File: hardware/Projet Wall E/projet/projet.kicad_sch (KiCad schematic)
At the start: 0 parts

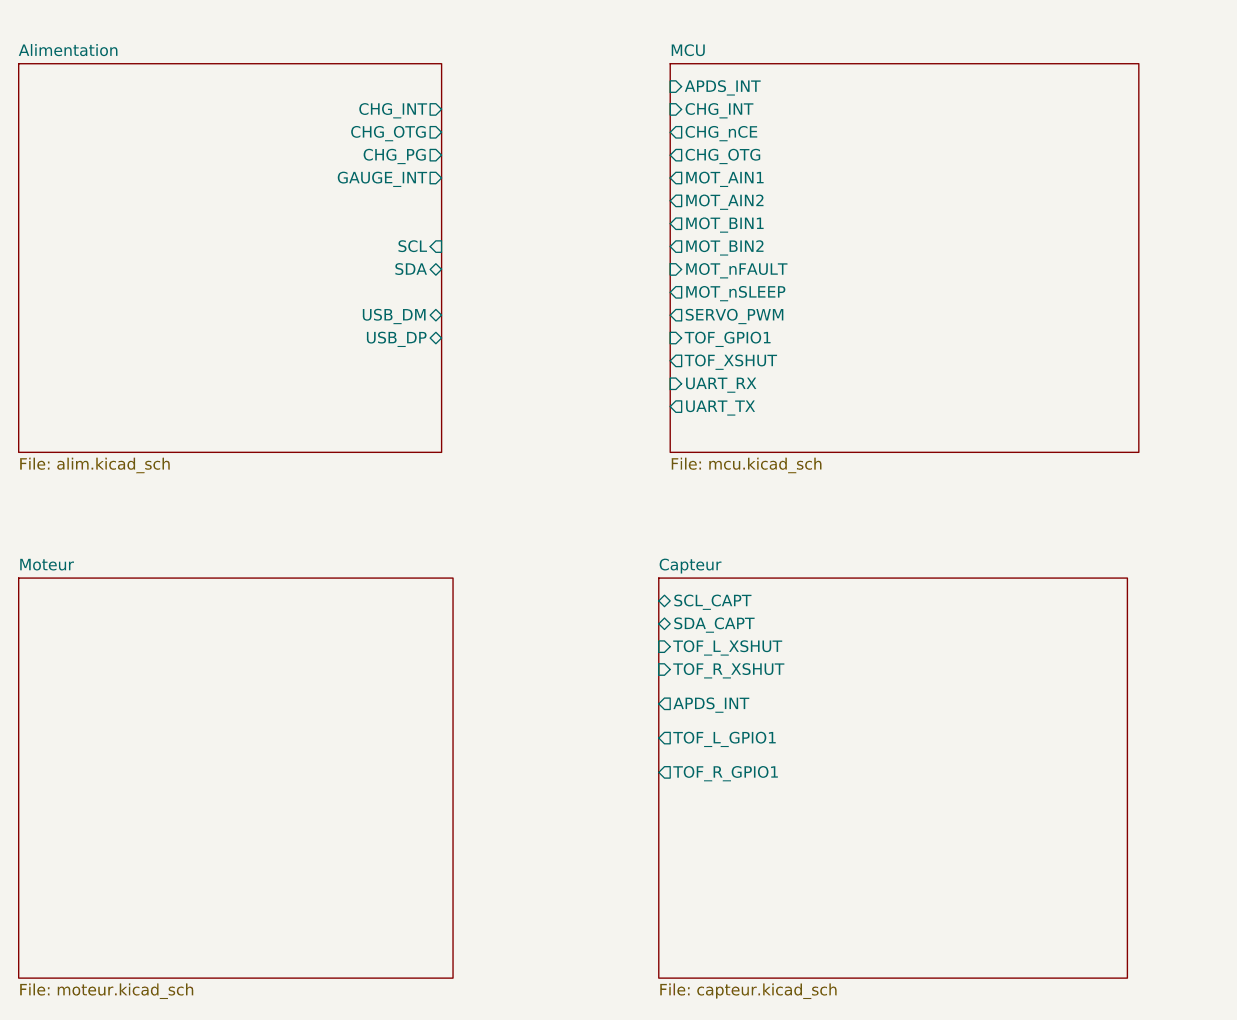
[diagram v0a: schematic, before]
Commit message: Feuille racine : liaisons hiérarchiques + corrections ERC
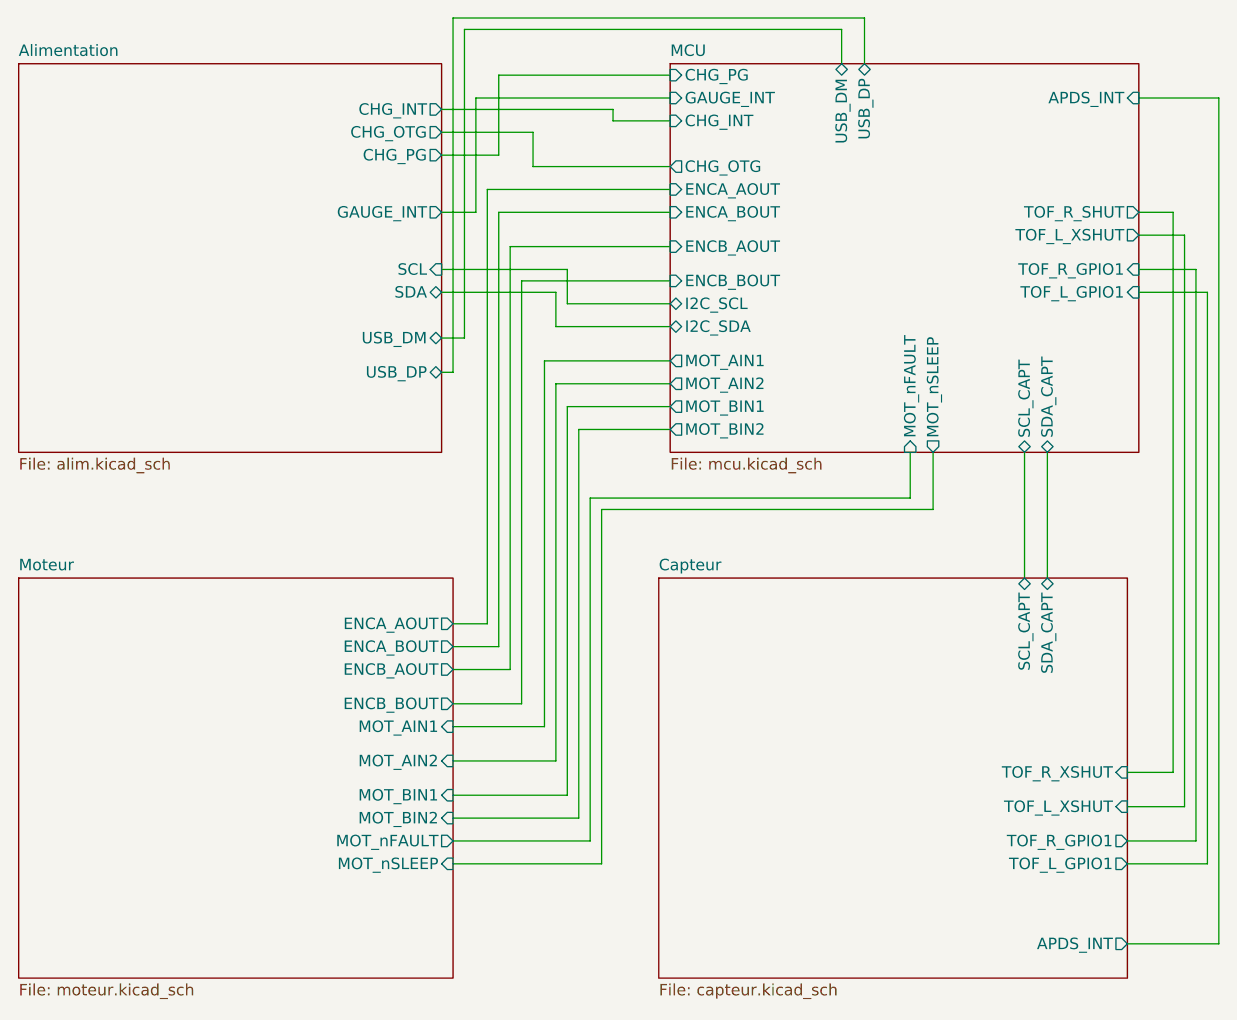
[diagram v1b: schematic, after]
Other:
- sheet MCU ports: added CHG_PG, ENCA_AOUT, ENCA_BOUT, ENCB_AOUT, ENCB_BOUT, GAUGE_INT, I2C_SCL, I2C_SDA, SCL_CAPT, SDA_CAPT, TOF_L_GPIO1, TOF_L_XSHUT, TOF_R_GPIO1, TOF_R_SHUT, USB_DM, USB_DP; removed CHG_nCE, SERVO_PWM, TOF_GPIO1, TOF_XSHUT, UART_RX, UART_TX
- sheet Moteur ports: added ENCA_AOUT, ENCA_BOUT, ENCB_AOUT, ENCB_BOUT, MOT_AIN1, MOT_AIN2, MOT_BIN1, MOT_BIN2, MOT_nFAULT, MOT_nSLEEP; removed none

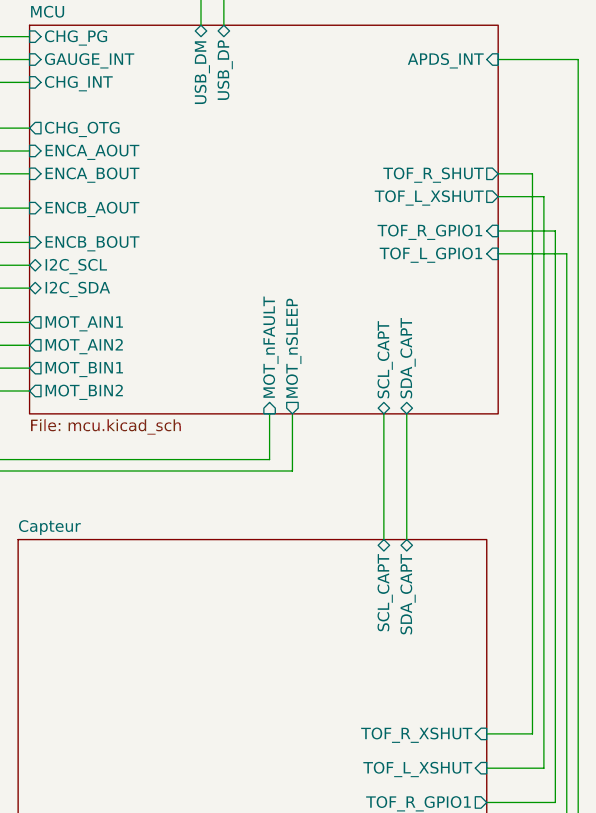
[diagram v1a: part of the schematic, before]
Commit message: Schéma : 0 erreur ERC, pinout MCU finalisé + config .ioc
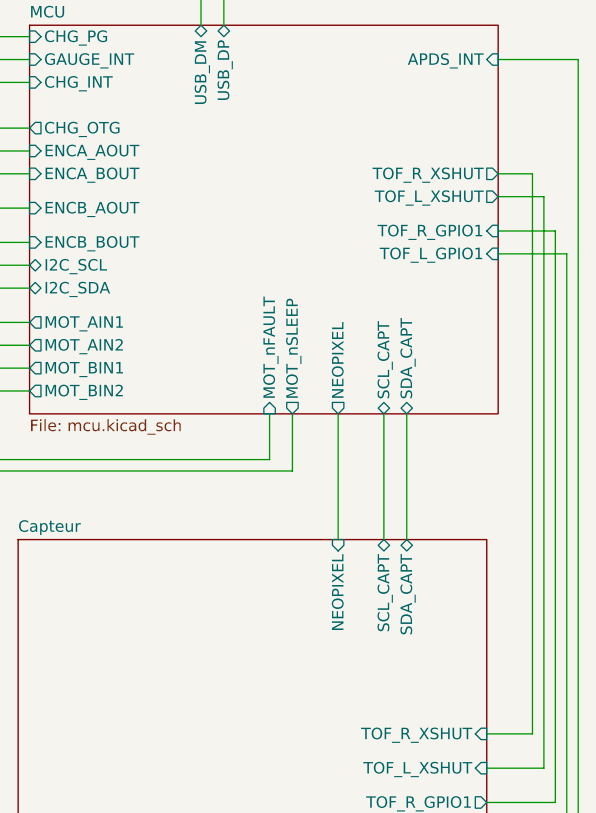
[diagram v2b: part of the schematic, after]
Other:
- sheet Capteur ports: added NEOPIXEL; removed none
- sheet MCU ports: added NEOPIXEL, TOF_R_XSHUT; removed TOF_R_SHUT
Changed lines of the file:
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@@
+	(wire
+		(pts
+			(xy 160.02 88.9) (xy 160.02 102.87)
+		)
+		(stroke
+			(width 0)
+			(type default)
+		)
+	)
 	(wire
 		(pts
@@
 			)
 		)
+		(pin "NEOPIXEL" input
+			(at 160.02 102.87 90)
+			(effects
+				(font
+					(size 1.27 1.27)
+				)
+				(justify right)
+			)
+		)
 		(instances
 			(project "projet"
@@
 			)
 		)
-		(pin "TOF_R_SHUT" output
-			(at 177.8 62.23 0)
-			(effects
-				(font
-					(size 1.27 1.27)
-				)
-				(justify right)
-			)
-		)
 		(pin "GAUGE_INT" input
 			(at 125.73 49.53 180)
@@
 			)
 		)
+		(pin "NEOPIXEL" output
+			(at 160.02 88.9 270)
+			(effects
+				(font
+					(size 1.27 1.27)
+				)
+				(justify left)
+			)
+		)
+		(pin "TOF_R_XSHUT" output
+			(at 177.8 62.23 0)
+			(effects
+				(font
+					(size 1.27 1.27)
+				)
+				(justify right)
+			)
+		)

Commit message: verification finale effectue
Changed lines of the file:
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@@
 			)
 		)
-		(pin "CHG_OTG" output
+		(pin "CHG_OTG" input
 			(at 125.73 57.15 180)
 			(effects
